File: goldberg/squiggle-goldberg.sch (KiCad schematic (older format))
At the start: 42 parts, among them SW1 switch, SW10 switch, SW11 switch, SW12 switch, SW13 switch, SW14 switch, SW15-1 switch, SW15-2 switch, SW16 switch, SW17 switch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

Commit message: Initial efforts towards adding I2C and LEDs
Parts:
- removed U2: ProMicro, footprints:promicro, symbol squiggle:promicro
- added U2: promicro-squiggle, footprints:promicro, symbol squiggle-goldberg-rescue:promicro-squiggle
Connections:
- net labels added: GND, SCL, VCC
- no-connect marks 13 -> 11
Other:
- moved on the sheet: U1
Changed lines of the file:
@@
 Comment4 ""
 $EndDescr
-NoConn ~ 6275 925
-NoConn ~ 6275 1025
-NoConn ~ 6275 1525
-NoConn ~ 7677 925
-NoConn ~ 7675 1125
-NoConn ~ 7675 1325
-NoConn ~ 7675 1525
-NoConn ~ 7675 1425
-NoConn ~ 6275 1325
-Text GLabel 6275 1625 0    50   Input ~ 0
-COL0
-Text GLabel 6275 1725 0    50   Input ~ 0
-COL1
-Text GLabel 6275 1825 0    50   Input ~ 0
-COL2
-Text GLabel 6275 1925 0    50   Input ~ 0
-COL3
-Text GLabel 6275 2025 0    50   Input ~ 0
-COL4
-Text GLabel 7675 2025 2    50   Input ~ 0
-ROW3
-Text GLabel 7675 1925 2    50   Input ~ 0
-ROW2
-Text GLabel 7675 1825 2    50   Input ~ 0
-ROW1
-Text GLabel 7675 1725 2    50   Input ~ 0
-ROW0
-NoConn ~ 7675 1625
 $Comp
 L squiggle:switch SW1
@@
 Wire Wire Line
 	1900 2200 1900 3700
-$Comp
-L squiggle:promicro U2
-U 1 1 5E2C8BA7
-P 6975 1675
-F 0 "U2" H 6975 2712 60  0000 C CNN
-F 1 "ProMicro" H 6975 2606 60  0000 C CNN
-F 2 "footprints:promicro" H 7075 625 60  0001 C CNN
-F 3 "" H 7075 625 60  0000 C CNN
-	1    6975 1675
-	1    0    0    -1
-$EndComp
-NoConn ~ 6275 1125
-NoConn ~ 6275 1225
-Text GLabel 6275 1425 0    50   Input ~ 0
-SDA
 Wire Wire Line
 	4350 2200 4350 2800
 Connection ~ 4350 2900
-NoConn ~ 9025 1175
-Text GLabel 9025 1075 2    50   Input ~ 0
+Text GLabel 9225 2525 2    50   Input ~ 0
 SDA
-$Comp
-L squiggle:trrs U1
-U 1 1 5E2CB886
-P 8675 975
-F 0 "U1" H 8903 1278 60  0000 L CNN
-F 1 "TRRS" H 8903 1172 60  0000 L CNN
-F 2 "footprints:trrs" H 8825 975 60  0001 C CNN
-F 3 "" H 8825 975 60  0001 C CNN
-	1    8675 975
-	-1   0    0    1
-$EndComp
-Wire Wire Line
-	7675 1025 8300 1025
-Wire Wire Line
-	8300 1025 8300 850
-Wire Wire Line
-	8300 850  9250 850
-Wire Wire Line
-	9250 850  9250 1275
-Wire Wire Line
-	9250 1275 9025 1275
-Wire Wire Line
-	7675 1225 8300 1225
-Wire Wire Line
-	8300 1225 8300 1500
-Wire Wire Line
-	8300 1500 9250 1500
-Wire Wire Line
-	9250 1500 9250 1375
-Wire Wire Line
-	9250 1375 9025 1375
 $Comp
 L squiggle:switch SW7
@@
 Wire Wire Line
 	3550 2900 3550 3700
+$Comp
+L power:VCC #PWR0101
+U 1 1 5F1A77F3
+P 10450 950
+F 0 "#PWR0101" H 10450 800 50  0001 C CNN
+F 1 "VCC" H 10465 1123 50  0000 C CNN
+F 2 "" H 10450 950 50  0001 C CNN
+F 3 "" H 10450 950 50  0001 C CNN
+	1    10450 950
+	1    0    0    -1
+$EndComp
+$Comp
+L power:PWR_FLAG #FLG0101
+U 1 1 5F1A8317
+P 10450 950
+F 0 "#FLG0101" H 10450 1025 50  0001 C CNN
+F 1 "PWR_FLAG" H 10450 1123 50  0000 C CNN
+F 2 "" H 10450 950 50  0001 C CNN
+F 3 "~" H 10450 950 50  0001 C CNN
+	1    10450 950
+	1    0    0    1
+$EndComp
+$Comp
+L power:PWR_FLAG #FLG0102
+U 1 1 5F1AF287
+P 10850 950
+F 0 "#FLG0102" H 10850 1025 50  0001 C CNN
+F 1 "PWR_FLAG" H 10850 1123 50  0000 C CNN
+F 2 "" H 10850 950 50  0001 C CNN
+F 3 "~" H 10850 950 50  0001 C CNN
+	1    10850 950
+	1    0    0    -1
+$EndComp
+$Comp
+L power:GND #PWR0102
+U 1 1 5F1AFA13
+P 10850 950
+F 0 "#PWR0102" H 10850 700 50  0001 C CNN
+F 1 "GND" H 10855 777 50  0000 C CNN
+F 2 "" H 10850 950 50  0001 C CNN
+F 3 "" H 10850 950 50  0001 C CNN
+	1    10850 950
+	1    0    0    -1
+$EndComp
+Text GLabel 6100 3050 0    50   Input ~ 0
+SDA
+Text GLabel 7500 3350 2    50   Input ~ 0
+ROW0
+Text GLabel 7500 3450 2    50   Input ~ 0
+ROW1
+Text GLabel 7500 3550 2    50   Input ~ 0
+ROW2
+Text GLabel 6100 3650 0    50   Input ~ 0
+COL4
+Text GLabel 6100 3550 0    50   Input ~ 0
+COL3
+Text GLabel 6100 3450 0    50   Input ~ 0
+COL2
+Text GLabel 6100 3350 0    50   Input ~ 0
+COL1
+Text GLabel 6100 3250 0    50   Input ~ 0
+COL0
+Text GLabel 7500 3650 2    50   Input ~ 0
+ROW3
+Wire Wire Line
+	7500 2650 8350 2650
+Wire Wire Line
+	8350 2650 8350 2350
+Wire Wire Line
+	8350 2350 9500 2350
+Wire Wire Line
+	8350 3000 8350 2850
+Wire Wire Line
+	8350 2850 7500 2850
+NoConn ~ 6100 2550
+NoConn ~ 6100 2650
+NoConn ~ 6100 2750
+NoConn ~ 6100 2850
+NoConn ~ 6100 3150
+NoConn ~ 7500 2550
+NoConn ~ 7500 2750
+NoConn ~ 7500 2950
+NoConn ~ 7500 3050
+NoConn ~ 7500 3150
+NoConn ~ 7500 3250
+$Comp
+L squiggle-goldberg-rescue:promicro-squiggle U2
+U 1 1 5F1D02CC
+P 6800 3300
+F 0 "U2" H 6800 4443 60  0000 C CNN
+F 1 "promicro-squiggle" H 6800 4337 60  0000 C CNN
+F 2 "footprints:promicro" H 6800 4231 60  0000 C CNN
+F 3 "" H 6900 2250 60  0000 C CNN
+	1    6800 3300
+	1    0    0    -1
+$EndComp
+Text GLabel 6100 2950 0    50   Input ~ 0
+SCL
+Text GLabel 9225 2625 2    50   Input ~ 0
+SCL
+$Comp
+L squiggle:trrs U1
+U 1 1 5E2CB886
+P 8875 2425
+F 0 "U1" H 9103 2728 60  0000 L CNN
+F 1 "TRRS" H 9103 2622 60  0000 L CNN
+F 2 "footprints:trrs" H 9025 2425 60  0001 C CNN
+F 3 "" H 9025 2425 60  0001 C CNN
+	1    8875 2425
+	-1   0    0    1
+$EndComp
+Wire Wire Line
+	9500 2350 9500 2725
+Wire Wire Line
+	9500 2725 9225 2725
+Wire Wire Line
+	9300 3000 9300 2825
+Wire Wire Line
+	9300 2825 9225 2825
+Wire Wire Line
+	9300 3000 8350 3000
 $EndSCHEMATC

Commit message: Added OLED
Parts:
- added JP1: L_GND, footprints:Jumper, symbol Device:Jumper
- added JP2: L_VCC, footprints:Jumper, symbol Device:Jumper
- added JP3: L_SCL, footprints:Jumper, symbol Device:Jumper
- added JP4: L_SDA, footprints:Jumper, symbol Device:Jumper
- added JP5: R_GND, footprints:Jumper, symbol Device:Jumper
- added JP6: R_VCC, footprints:Jumper, symbol Device:Jumper
- added JP7: R_SCL, footprints:Jumper, symbol Device:Jumper
- added JP8: R_SDA, footprints:Jumper, symbol Device:Jumper
- added P1: OLED, footprints:SSD_1306_128x32, symbol this_keeb:CONN_01X04
- added R1, R2: 4.7K, Resistor_THT:R_Axial_DIN0207_L6.3mm_D2.5mm_P10.16mm_Horizontal, symbol Device:R_Small
- SW1, SW10, SW11, SW12, SW13, SW14, SW15-1, SW15-2, SW16, SW17, SW18, SW19-1, SW19-2, SW2, SW3, SW4, SW5, SW6, SW7, SW8, SW9: symbol squiggle:switch -> squiggle-goldberg-rescue:switch-squiggle
- U1: symbol squiggle:trrs -> squiggle-goldberg-rescue:trrs-squiggle
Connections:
- net GND: now also U1.2 (TIP), U2.23 (GND), U2.3 (GND), U2.4 (GND), JP1.2, JP5.2
- net SCL: now also U2.6 (SCL), JP3.2, JP7.2, R1.2; no longer U1.4 (RING2), U2.5 (SDA)
- net SDA: now also U2.5 (SDA), JP4.2, JP8.2, R2.2; no longer U1.1 (SLEEVE), U2.6 (SCL)
- net VCC: now also U1.1 (SLEEVE), U2.21 (VCC), JP2.2, JP6.2, R1.1, R2.1
- net DATA: now reaches U1.3 (RING1)
- net DATA: now also U2.2 (RX); no longer U2.23 (GND)
- new net: JP1.1, JP8.1, P1.1 (P1)
- new net: JP2.1, JP7.1, P1.2 (P2)
- new net: JP3.1, JP6.1, P1.3 (P3)
- new net: JP4.1, JP5.1, P1.4 (P4)
- no-connect marks 11 -> 9
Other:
- moved on the sheet: U1, U2

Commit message: PC change
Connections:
- net LED: now reaches U2.1 (TX)
- no-connect marks 9 -> 8
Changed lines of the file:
@@
 Text GLabel 8400 5800 2    50   Input ~ 0
 ROW3
-NoConn ~ 7000 4700
 NoConn ~ 7000 5300
 NoConn ~ 8400 4700
@@
 	1125 5350 1825 5350
 Connection ~ 1125 6750
+Text GLabel 7000 4700 0    50   Input ~ 0
+LED
 $EndSCHEMATC

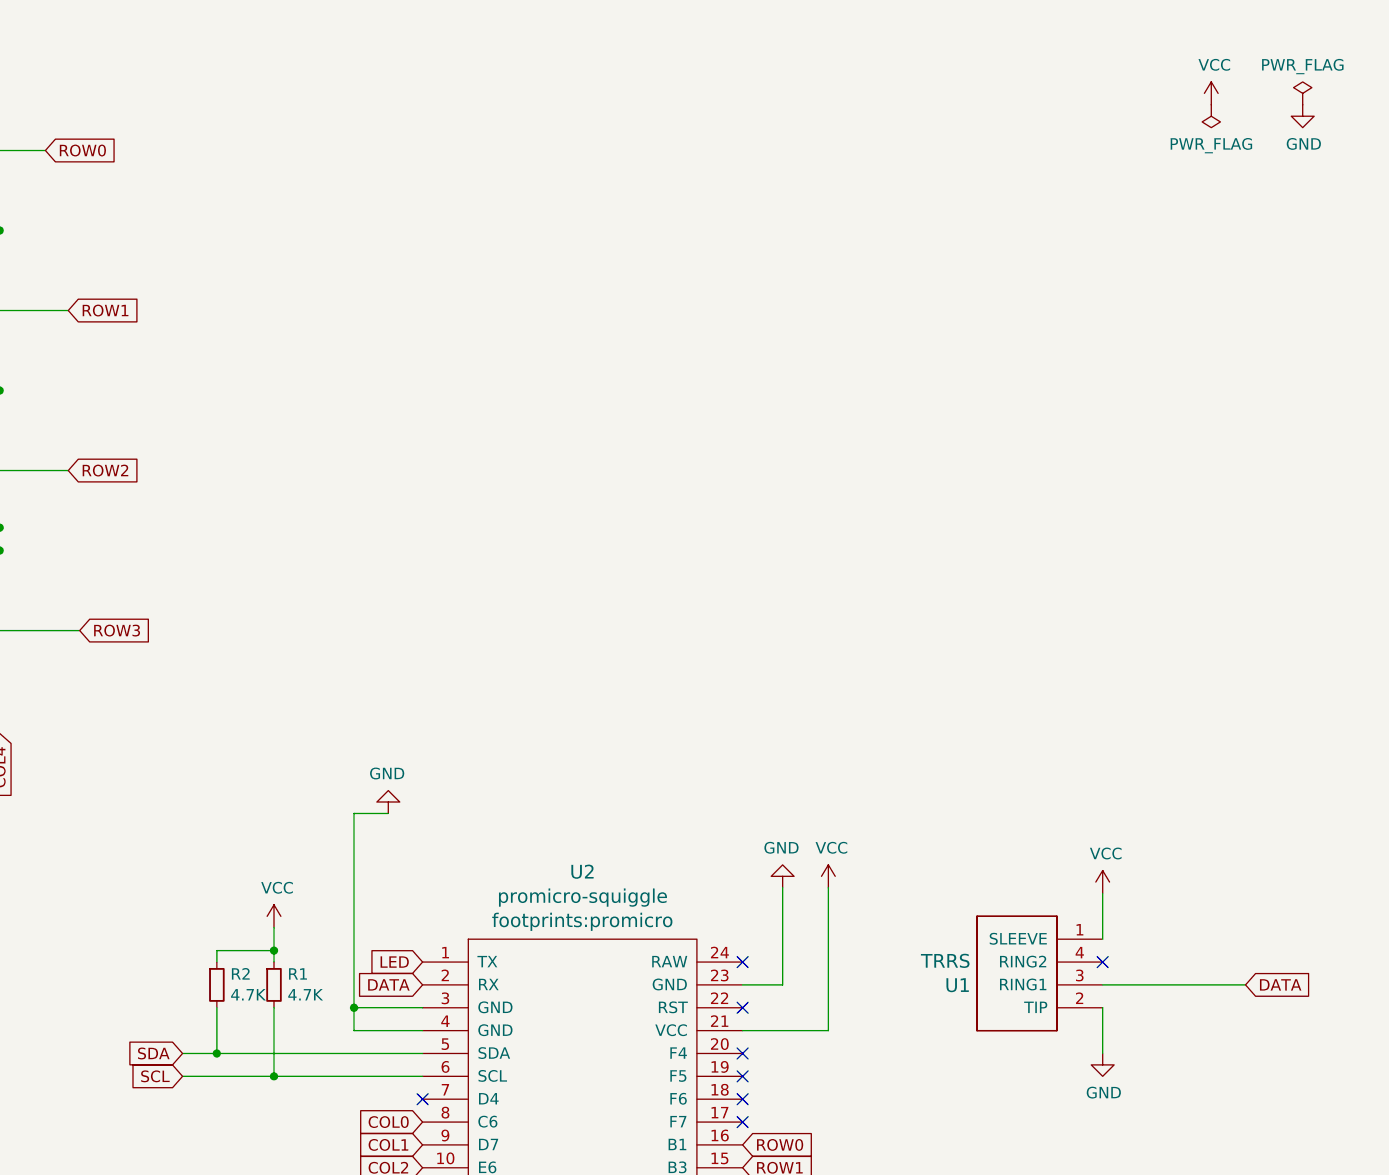
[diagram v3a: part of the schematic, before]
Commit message: Added LEDs and RESET button
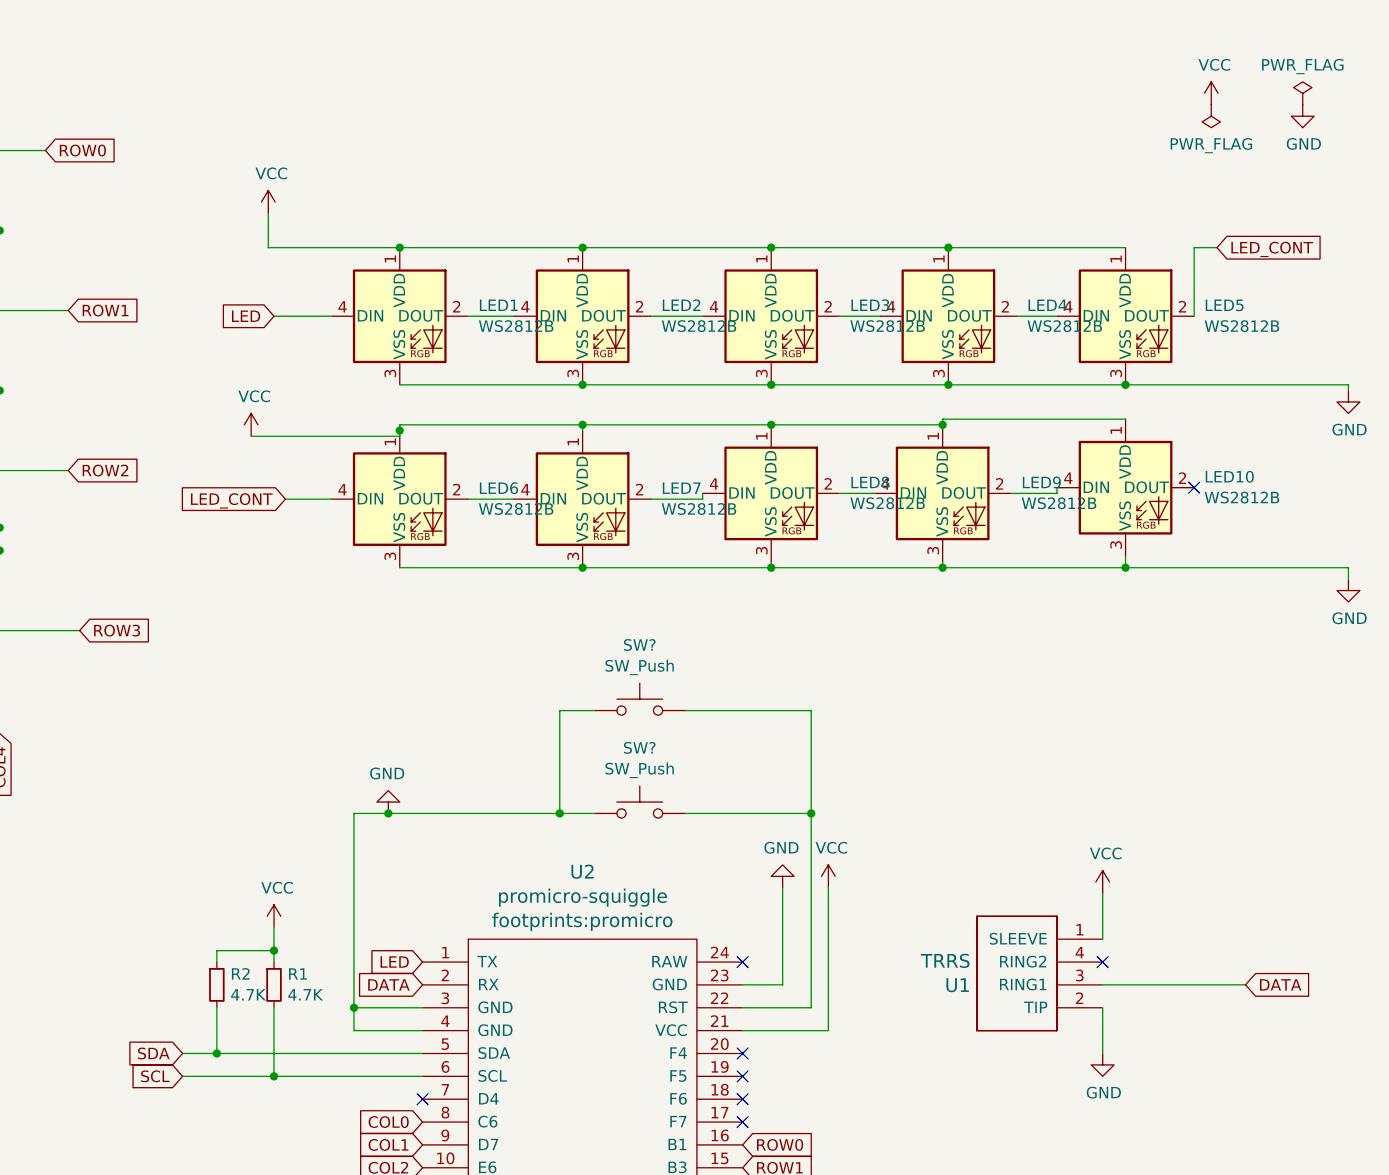
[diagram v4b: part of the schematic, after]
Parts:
- added LED1, LED10, LED2, LED3, LED4, LED5, LED6, LED7, LED8, LED9: WS2812B, footprints:LED_WS2812B_4Pad, symbol LED:WS2812B
- added SW? (x2): SW_Push, Button_Switch_THT:SW_PUSH_6mm_H5mm, symbol Switch:SW_Push
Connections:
- net GND: now also LED1.3 (VSS), LED10.3 (VSS), LED2.3 (VSS), LED3.3 (VSS), LED4.3 (VSS), LED5.3 (VSS), LED6.3 (VSS), LED7.3 (VSS), LED8.3 (VSS), LED9.3 (VSS), SW?.1, SW?.1
- net LED: now also LED1.4 (DIN)
- net VCC: now also LED1.1 (VDD), LED10.1 (VDD), LED2.1 (VDD), LED3.1 (VDD), LED4.1 (VDD), LED5.1 (VDD), LED6.1 (VDD), LED7.1 (VDD), LED8.1 (VDD), LED9.1 (VDD)
- net at U2.22 (RST): now also SW?.2, SW?.2
- new net: LED1.2 (DOUT), LED2.4 (DIN)
- new net: LED2.2 (DOUT), LED3.4 (DIN)
- new net: LED3.2 (DOUT), LED4.4 (DIN)
- new net: LED4.2 (DOUT), LED5.4 (DIN)
- new net: LED6.2 (DOUT), LED7.4 (DIN)
- new net: LED7.2 (DOUT), LED8.4 (DIN)
- new net: LED8.2 (DOUT), LED9.4 (DIN)
- new net: LED10.4 (DIN), LED9.2 (DOUT)
- new net LED_CONT: LED5.2 (DOUT), LED6.4 (DIN)

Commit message: PC change
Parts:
- gave numbers to parts that had none: 2
